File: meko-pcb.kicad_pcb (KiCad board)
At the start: 2 copper layers, 23 parts, among them IC1 ES9218PQ, IC2 AS5600-ASOM, IC3 TPS7A8701RTJT, IC4 TPS7A8701RTJT, J1 FH34SRJ-24S-0.5SH_99_, J2 MEM2090-00-145-00-A, J3 USB_C_Receptacle_USB2.0_16P, U1 ESP32-PICO-MINI-02, U12 BQ24075RGT, U4 CP2102N-Axx-xQFN20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

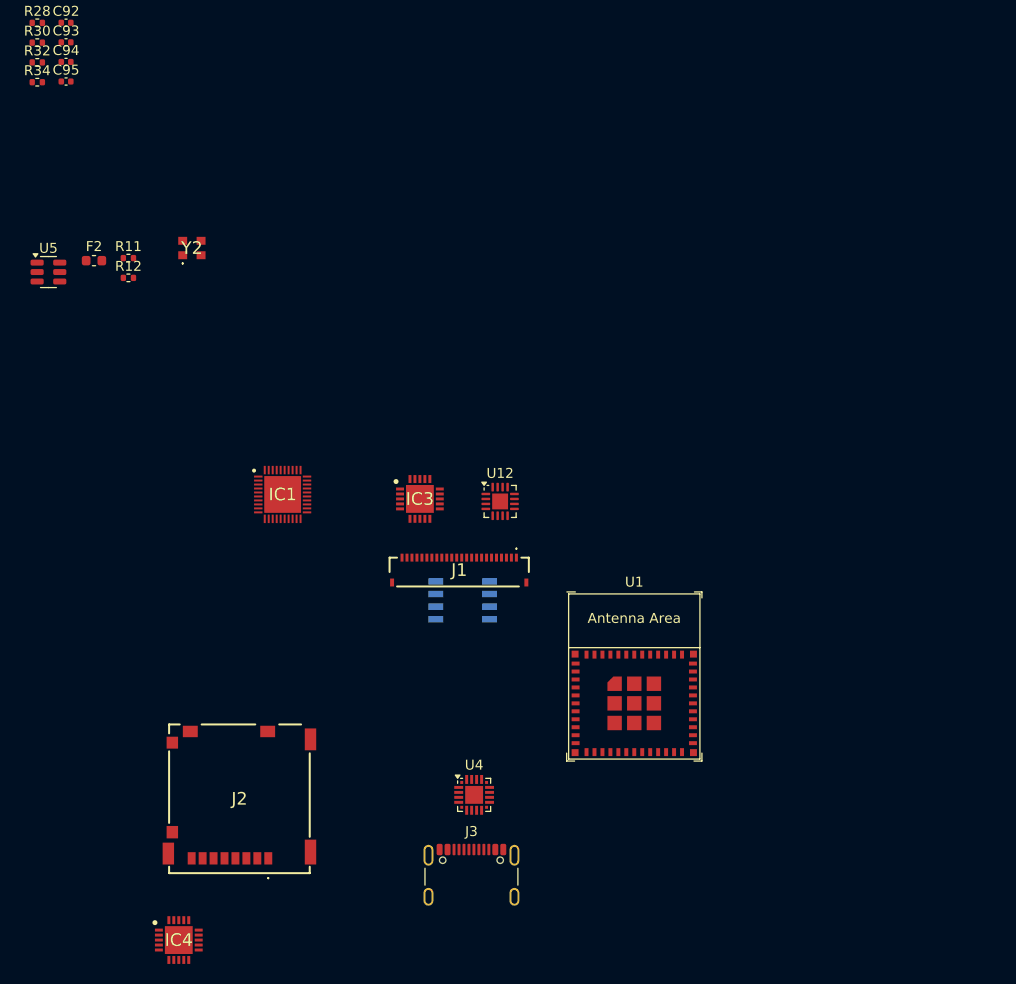
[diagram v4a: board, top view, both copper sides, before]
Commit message: re-did power with the new small LDOs and power system
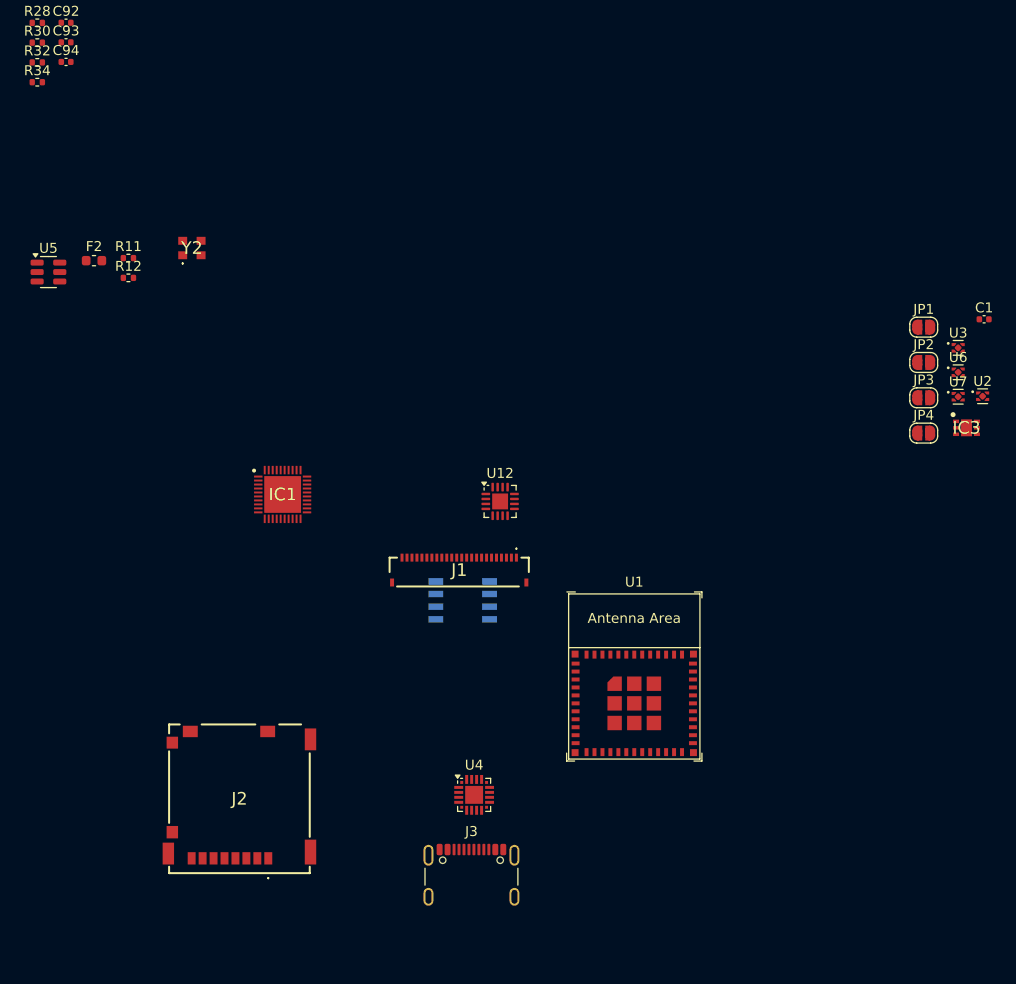
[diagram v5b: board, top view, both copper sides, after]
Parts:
- removed C95: 4.7uF, Capacitor_SMD:C_0402_1005Metric
- removed IC4: TPS7A8701RTJT, TPS7A8701RTJT:QFN50P400X400X80-21N-D
- added C1: 4.7uF, Capacitor_SMD:C_0402_1005Metric, F.Cu at (218.7, 91.9)
- added JP1: SolderJumper_2_Open, Jumper:SolderJumper-2_P1.3mm_Open_RoundedPad1.0x1.5mm, F.Cu at (212.7, 92.7)
- added JP2: SolderJumper_2_Open, Jumper:SolderJumper-2_P1.3mm_Open_RoundedPad1.0x1.5mm, F.Cu at (212.7, 96.3)
- added JP3: SolderJumper_2_Open, Jumper:SolderJumper-2_P1.3mm_Open_RoundedPad1.0x1.5mm, F.Cu at (212.7, 99.8)
- added JP4: SolderJumper_2_Open, Jumper:SolderJumper-2_P1.3mm_Open_RoundedPad1.0x1.5mm, F.Cu at (212.7, 103.4)
- added U2: LP5907SNX-1.8/NOPB, Package_SON:Texas_X2SON-4_1x1mm_P0.65mm, F.Cu at (218.6, 99.7)
- added U3: LP5907SNX-3.3/NOPB, Package_SON:Texas_X2SON-4_1x1mm_P0.65mm, F.Cu at (216.1, 94.8)
- added U6: LP5907SNX-3.3/NOPB, Package_SON:Texas_X2SON-4_1x1mm_P0.65mm, F.Cu at (216.1, 97.3)
- added U7: LP5907SNX-3.3/NOPB, Package_SON:Texas_X2SON-4_1x1mm_P0.65mm, F.Cu at (216.1, 99.7)
- IC3: value TPS7A8701RTJT -> LP5912-3.3DRVR; footprint TPS7A8701RTJT:QFN50P400X400X80-21N-D -> LP5912-3.3DRVR:SON65P200X200X80-7N
- moved IC3 55.4 mm to (216.9, 102.8)
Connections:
- IC3 pad 1: /power/REG-OUT -> +3V3
- IC3 pad 2: /power/REG-OUT -> unconnected-(IC3-NC-Pad2)
- IC3 pad 3: GND -> unconnected-(IC3-PG-Pad3)
- IC3 pad 5: /power/REG-OUT -> GND
- IC3 pad 6: unconnected-(IC3-EN2-Pad6) -> /power/REG-OUT
- IC3 pad 7: unconnected-(IC3-NR/SS2-Pad7) -> GND
- U1 pad 1: Net-(U1-GND-Pad1) -> GND
- U1 pad 11: Net-(U1-GND-Pad1) -> GND
- U1 pad 14: Net-(U1-GND-Pad1) -> GND
- U1 pad 2: Net-(U1-GND-Pad1) -> GND
- U1 pad 36: Net-(U1-GND-Pad1) -> GND
- U1 pad 37: Net-(U1-GND-Pad1) -> GND
- U1 pad 38: Net-(U1-GND-Pad1) -> GND
- U1 pad 39: Net-(U1-GND-Pad1) -> GND
- U1 pad 40: Net-(U1-GND-Pad1) -> GND
- U1 pad 41: Net-(U1-GND-Pad1) -> GND
- U1 pad 42: Net-(U1-GND-Pad1) -> GND
- U1 pad 43: Net-(U1-GND-Pad1) -> GND
- U1 pad 44: Net-(U1-GND-Pad1) -> GND
- U1 pad 45: Net-(U1-GND-Pad1) -> GND
- U1 pad 46: Net-(U1-GND-Pad1) -> GND
- U1 pad 47: Net-(U1-GND-Pad1) -> GND
- U1 pad 48: Net-(U1-GND-Pad1) -> GND
- U1 pad 49: Net-(U1-GND-Pad1) -> GND
- U1 pad 50: Net-(U1-GND-Pad1) -> GND
- U1 pad 51: Net-(U1-GND-Pad1) -> GND
- U1 pad 52: Net-(U1-GND-Pad1) -> GND
- U1 pad 53: Net-(U1-GND-Pad1) -> GND
- Y2 pad 4: +1V8 -> unconnected-(Y2-VDD-Pad4)

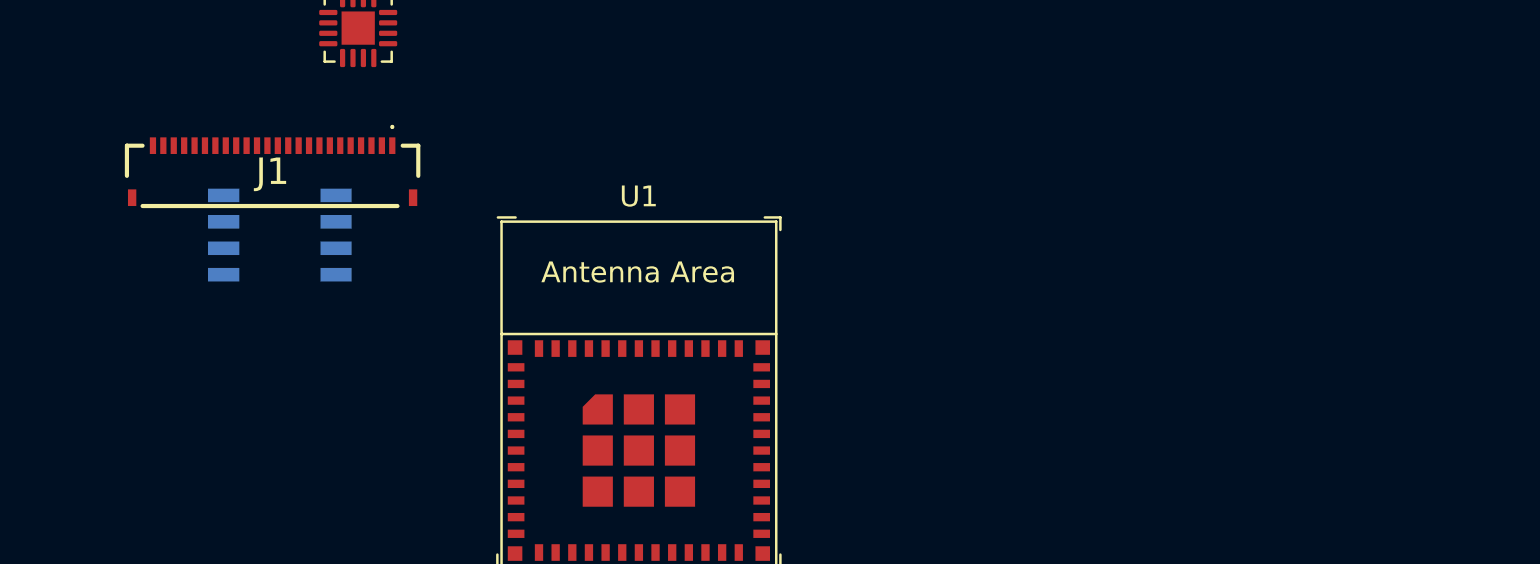
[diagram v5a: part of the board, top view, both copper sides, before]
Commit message: created custom symbol for the display, added pull-up/-down resistors
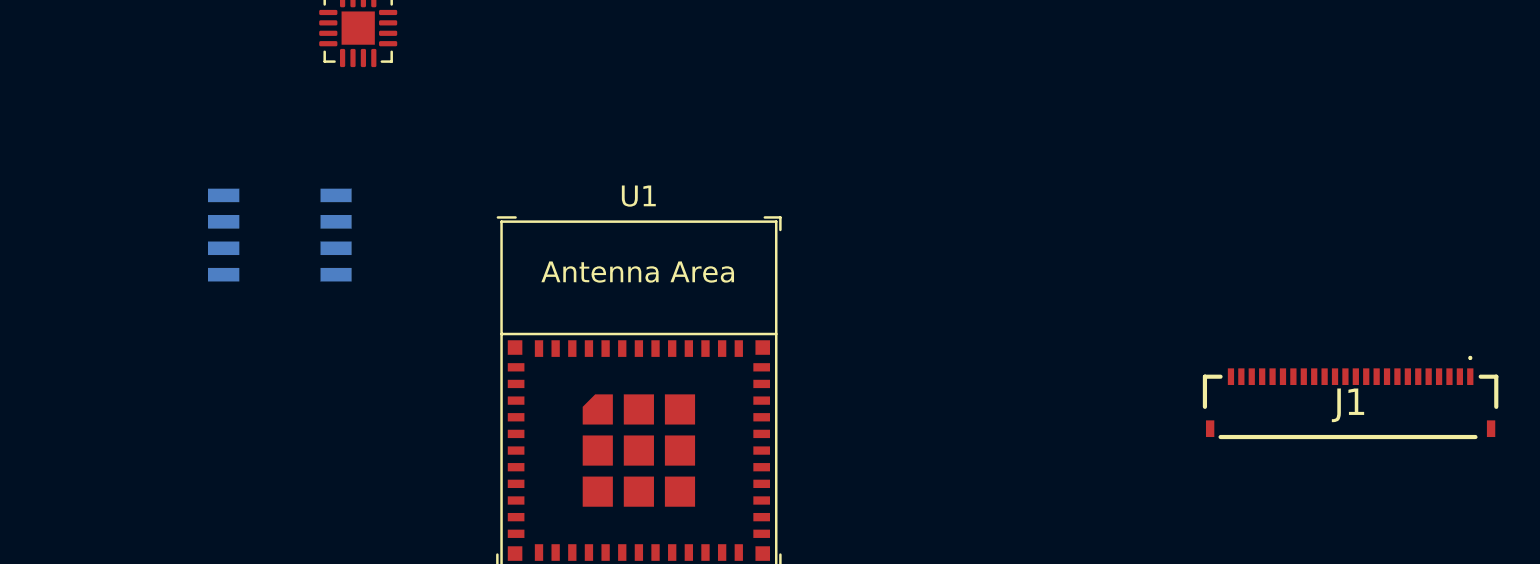
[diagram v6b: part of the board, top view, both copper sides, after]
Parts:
- J1: value FH34SRJ-24S-0.5SH_99_ -> GDEY0154D67
- moved J1 53.0 mm to (217.8, 128.4)
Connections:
- IC1 pad 19: +1V8 -> +1V8AVCC
- IC1 pad 20: +3V3 -> +3V3AVCC
- IC1 pad 29: +1V8 -> +3V3AVDD
- IC1 pad 4: +3V3 -> +3V3VCCA
- IC2 pad 2: unconnected-(IC2-VDD3V3-Pad2) -> +3V3
- J1 pad MP1: unconnected-(J1-PadMP1) -> GND
- J1 pad MP2: unconnected-(J1-PadMP2) -> GND
- J2 pad 10: unconnected-(J2-GROUND_1-Pad10) -> GND
- J2 pad 11: unconnected-(J2-GROUND_2-Pad11) -> GND
- J2 pad 12: unconnected-(J2-GROUND_3-Pad12) -> GND
- J2 pad 13: unconnected-(J2-GROUND_4-Pad13) -> GND
- J2 pad 14: unconnected-(J2-GROUND_5-Pad14) -> GND
- J2 pad 15: unconnected-(J2-GROUND_6-Pad15) -> GND
- U1 pad 3: unconnected-(U1-3V3-Pad3) -> +3V3
- Y2 pad 4: unconnected-(Y2-VDD-Pad4) -> +3V3MCLK

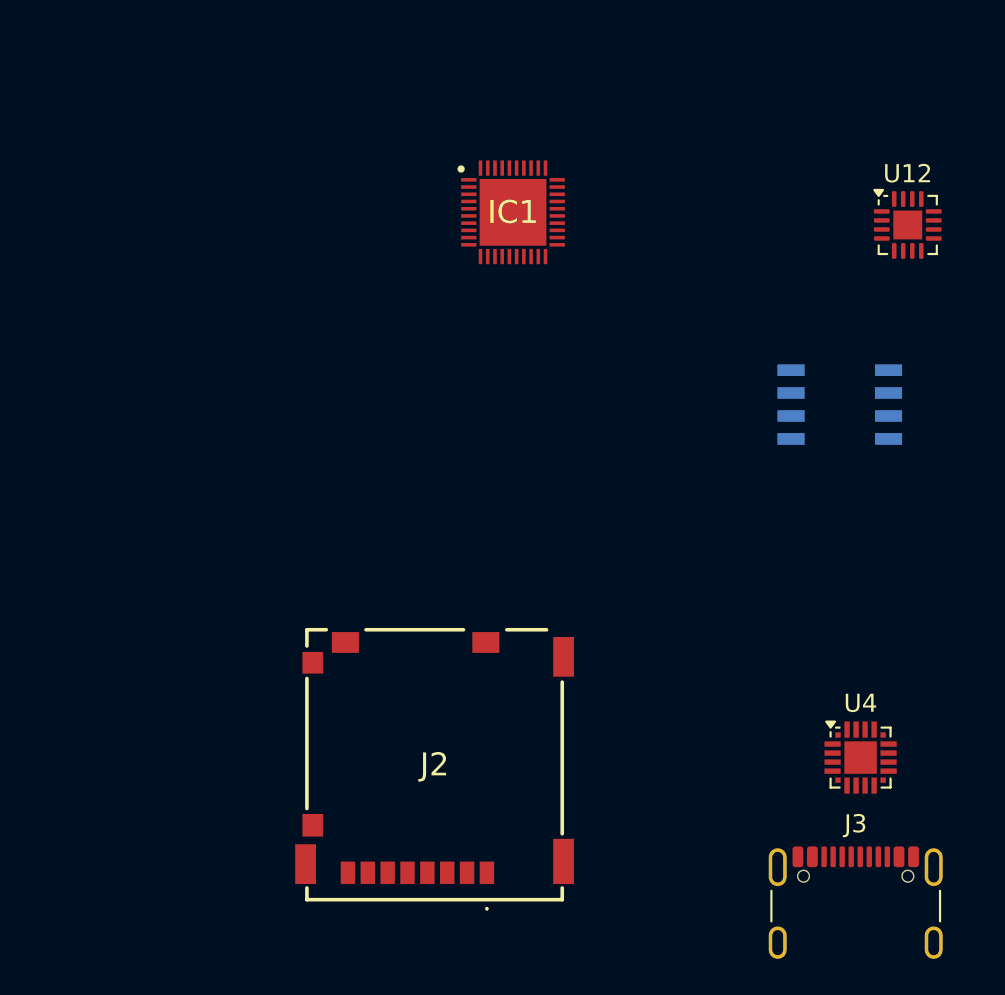
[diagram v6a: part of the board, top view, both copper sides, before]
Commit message: i2c, i2s, uart, en, sd card
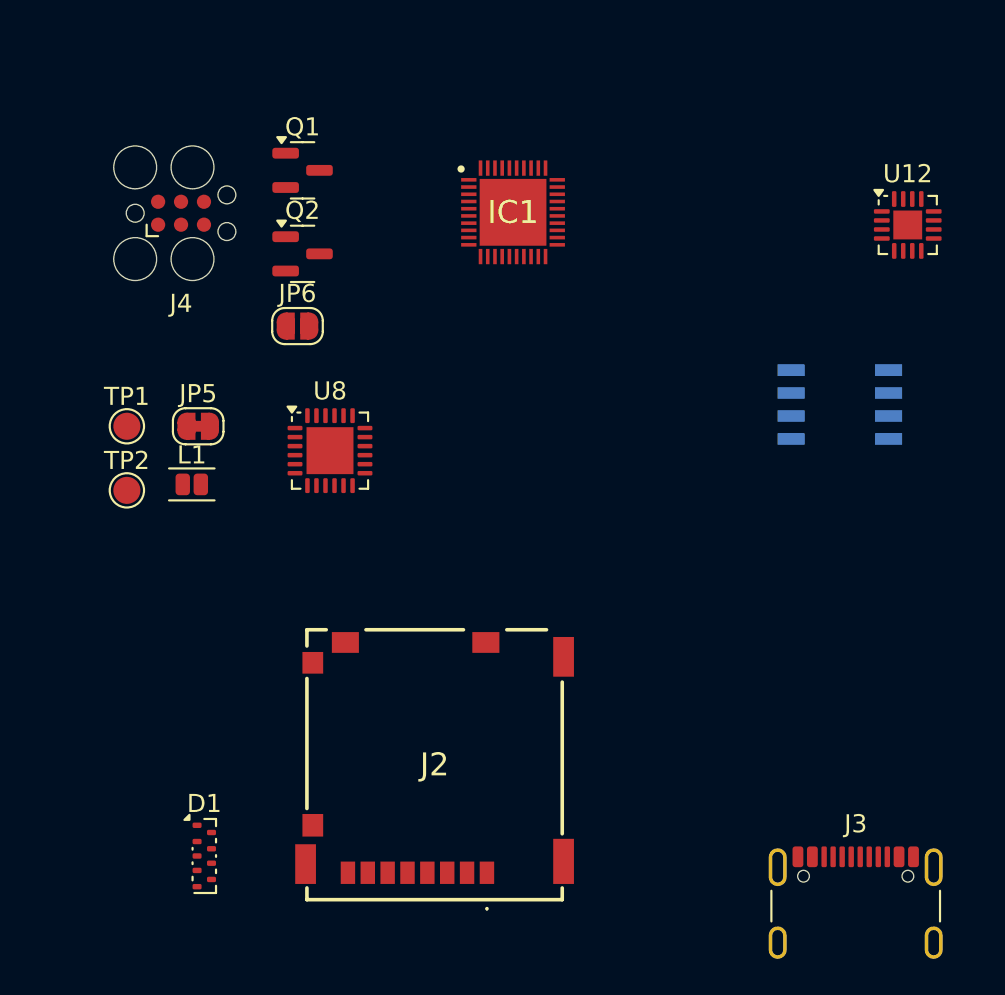
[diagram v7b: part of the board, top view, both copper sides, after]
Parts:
- removed U4: CP2102N-Axx-xQFN20, Package_DFN_QFN:SiliconLabs_QFN-20-1EP_3x3mm_P0.5mm_EP1.8x1.8mm
- added D1: D3V3X8U9LP3810, Package_DFN_QFN:Diodes_UDFN3810-9_TYPE_B, F.Cu at (131.1, 145.2)
- added J4: Conn_ARM_SWD_TagConnect_TC2030, Connector:Tag-Connect_TC2030-IDC-FP_2x03_P1.27mm_Vertical, F.Cu at (129.8, 109.6)
- added JP5: SolderJumper_2_Bridged, Jumper:SolderJumper-2_P1.3mm_Bridged_RoundedPad1.0x1.5mm, F.Cu at (130.8, 121.4)
- added JP6: SolderJumper_2_Open, Jumper:SolderJumper-2_P1.3mm_Open_RoundedPad1.0x1.5mm, F.Cu at (136.3, 115.8)
- added L1: 100uH, Inductor_SMD:L_TDK_MLZ2012_h1.25mm, F.Cu at (130.4, 124.6)
- added Q1: SS8050, Package_TO_SOT_SMD:SOT-23, F.Cu at (136.5, 107.2)
- added Q2: SS8050, Package_TO_SOT_SMD:SOT-23, F.Cu at (136.5, 111.8)
- added TP1: TestPoint, TestPoint:TestPoint_Pad_D1.5mm, F.Cu at (126.8, 121.4)
- added TP2: TestPoint, TestPoint:TestPoint_Pad_D1.5mm, F.Cu at (126.8, 125.0)
- added U8: CP2102N-Axx-xQFN24, Package_DFN_QFN:QFN-24-1EP_4x4mm_P0.5mm_EP2.6x2.6mm, F.Cu at (138.1, 122.8)
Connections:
- net /audio/DATA_CLK renamed /AUDIO_DATA_CLK
- IC1 pad 34: /audio/DATA_2 -> /AUDIO_DATA_2
- IC1 pad 35: /audio/DATA1 -> /AUDIO_DATA1
- IC1 pad 38: /audio/SCL -> /AUDIO_SCL
- IC1 pad 39: /audio/SDA -> /AUDIO_SDA
- IC2 pad 3: unconnected-(IC2-OUT-Pad3) -> /HAL_OUT
- IC2 pad 4: unconnected-(IC2-GND-Pad4) -> GND
- IC2 pad 5: unconnected-(IC2-PGO-Pad5) -> Net-(IC2-PGO)
- IC2 pad 6: unconnected-(IC2-SDA-Pad6) -> /HAL_SDA
- IC2 pad 7: unconnected-(IC2-SCL-Pad7) -> /HAL_SCL
- IC2 pad 8: unconnected-(IC2-DIR-Pad8) -> GND
- J2 pad 1: unconnected-(J2-DAT2-Pad1) -> /MEM_DAT2
- J2 pad 2: unconnected-(J2-CD/DAT3-Pad2) -> /MEM_DAT3
- J2 pad 3: unconnected-(J2-CMD-Pad3) -> /MEM_CMD
- J2 pad 4: unconnected-(J2-VDD-Pad4) -> +3V3
- J2 pad 5: unconnected-(J2-CLK-Pad5) -> /MEM_CLK
- J2 pad 6: unconnected-(J2-VSS-Pad6) -> GND
- J2 pad 7: unconnected-(J2-DAT0-Pad7) -> /MEM_DAT0
- J2 pad 8: unconnected-(J2-DAT1-Pad8) -> /MEM_DAT1
- J2 pad 9: unconnected-(J2-COM-Pad9) -> /MEM_COM
- U1 pad 15: unconnected-(U1-GPIO25/ADC2_CH8/DAC_1-Pad15) -> /AUDIO_SCL
- U1 pad 16: unconnected-(U1-GPIO26/ADC2_CH9/DAC_2-Pad16) -> /AUDIO_SDA
- U1 pad 18: unconnected-(U1-MTMS/GPIO14/ADC2_CH6-Pad18) -> /MEM_CLK
- U1 pad 19: unconnected-(U1-MTDI/GPIO12/ADC2_CH5-Pad19) -> /MEM_DAT2
- U1 pad 20: unconnected-(U1-MTCK/GPIO13/ADC2_CH4-Pad20) -> /MEM_DAT3
- U1 pad 21: unconnected-(U1-MTDO/GPIO15/ADC2_CH3-Pad21) -> /MEM_CMD
- U1 pad 22: unconnected-(U1-GPIO2/ADC2_CH2-Pad22) -> /MEM_DAT0
- U1 pad 23: unconnected-(U1-GPIO0/BOOT/ADC2_CH1-Pad23) -> /BOOT
- U1 pad 24: unconnected-(U1-GPIO4/ADC2_CH0-Pad24) -> /MEM_DAT1
- U1 pad 26: unconnected-(U1-GPIO20-Pad26) -> /HAL_SDA
- U1 pad 30: unconnected-(U1-U0RXD/GPIO3-Pad30) -> /RXD
- U1 pad 31: unconnected-(U1-U0TXD/GPIO1-Pad31) -> /TXD
- U1 pad 33: unconnected-(U1-GPIO19-Pad33) -> /HAL_SCL
- U1 pad 34: unconnected-(U1-GPIO22-Pad34) -> /AUDIO_DATA_2
- U1 pad 35: unconnected-(U1-GPIO21-Pad35) -> /AUDIO_DATA1
- U1 pad 4: unconnected-(U1-SENSOR_VP/GPIO36/ADC1_CH0-Pad4) -> /HAL_OUT
- U1 pad 8: unconnected-(U1-EN/CHIP_PU-Pad8) -> /ESP_EN
- U12 pad 6: +5V -> Net-(JP5-B)
- U12 pad 7: unconnected-(U12-~{PGOOD}-Pad7) -> Net-(U12-~{PGOOD})
- U12 pad 9: unconnected-(U12-~{CHG}-Pad9) -> Net-(U12-~{CHG})

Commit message: finishing up schematic
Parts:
- added D2: MBR0530, Diode_SMD:D_SOD-123, F.Cu at (202.3, 118.5)
- added D3: MBR0530, Diode_SMD:D_SOD-123, F.Cu at (245.2, 126.9)
- added D4: MBR0530, Diode_SMD:D_SOD-123, F.Cu at (245.2, 130.3)
- added J5: SJ2-35954B-SMT-TR, SJ2-35954B-SMT-TR:CUI_SJ2-35954B-SMT-TR, F.Cu at (76.8, 74.8)
- added JP7: SolderJumper_2_Bridged, Jumper:SolderJumper-2_P1.3mm_Bridged_RoundedPad1.0x1.5mm, F.Cu at (125.3, 146.0)
- added JP8: SolderJumper_2_Bridged, Jumper:SolderJumper-2_P1.3mm_Bridged_RoundedPad1.0x1.5mm, F.Cu at (240.1, 130.6)
- added JP9: SolderJumper_2_Bridged, Jumper:SolderJumper-2_P1.3mm_Bridged_RoundedPad1.0x1.5mm, F.Cu at (70.2, 82.3)
- added L2: 47uF, Inductor_SMD:L_TDK_MLZ2012_h1.25mm, F.Cu at (239.7, 133.8)
- added Q3: Si1308EDL, Package_TO_SOT_SMD:SOT-323_SC-70, F.Cu at (244.5, 134.0)
- added TP10: TestPoint, TestPoint:TestPoint_Pad_D1.5mm, F.Cu at (77.0, 91.5)
- added TP11: TestPoint, TestPoint:TestPoint_Pad_D1.5mm, F.Cu at (77.0, 95.0)
- added TP12: TestPoint, TestPoint:TestPoint_Pad_D1.5mm, F.Cu at (80.5, 87.9)
- added TP13: TestPoint, TestPoint:TestPoint_Pad_D1.5mm, F.Cu at (80.5, 91.5)
- added TP14: TestPoint, TestPoint:TestPoint_Pad_D1.5mm, F.Cu at (80.5, 95.0)
- added TP3: TestPoint, TestPoint:TestPoint_Pad_D1.5mm, F.Cu at (69.8, 87.9)
- added TP4: TestPoint, TestPoint:TestPoint_Pad_D1.5mm, F.Cu at (69.8, 91.5)
- added TP5: TestPoint, TestPoint:TestPoint_Pad_D1.5mm, F.Cu at (69.8, 95.0)
- added TP6: TestPoint, TestPoint:TestPoint_Pad_D1.5mm, F.Cu at (73.4, 87.9)
- added TP7: TestPoint, TestPoint:TestPoint_Pad_D1.5mm, F.Cu at (73.4, 91.5)
- added TP8: TestPoint, TestPoint:TestPoint_Pad_D1.5mm, F.Cu at (73.4, 95.0)
- added TP9: TestPoint, TestPoint:TestPoint_Pad_D1.5mm, F.Cu at (77.0, 87.9)
- JP1, JP2, JP3, JP4: value SolderJumper_2_Open -> SolderJumper_2_Bridged; footprint Jumper:SolderJumper-2_P1.3mm_Open_RoundedPad1.0x1.5mm -> Jumper:SolderJumper-2_P1.3mm_Bridged_RoundedPad1.0x1.5mm
- moved JP1 126.4 mm to (88.0, 71.3)
- moved JP2 126.4 mm to (88.0, 74.9)
- moved JP3 126.4 mm to (88.0, 78.4)
- moved JP4 126.4 mm to (88.0, 82.0)
- moved R34 57.9 mm to (164.0, 109.5)
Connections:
- IC1 pad 37: /audio/RESETB -> /AUDIO_RESETB
- IC2 pad 1: unconnected-(IC2-VDD5V-Pad1) -> Net-(IC2-VDD5V)
- J1 pad 10: unconnected-(J1-~{RES}-Pad10) -> /DISPL_~{RES}
- J1 pad 11: unconnected-(J1-~{D/C}-Pad11) -> /DISPL_~{D/C}
- J1 pad 12: unconnected-(J1-~{CS}-Pad12) -> /DISPL_~{CS}
- J1 pad 13: unconnected-(J1-SCL-Pad13) -> /DISPL_SCL
- J1 pad 14: unconnected-(J1-SDA-Pad14) -> /DISPL_SDA
- J1 pad 15: unconnected-(J1-VDDIO-Pad15) -> +3V3
- J1 pad 16: unconnected-(J1-VCI-Pad16) -> +3V3
- J1 pad 17: unconnected-(J1-VSS-Pad17) -> GND
- J1 pad 18: unconnected-(J1-VDD-Pad18) -> Net-(J1-VDD)
- J1 pad 2: unconnected-(J1-GDR-Pad2) -> /DISPL_GDR
- J1 pad 20: unconnected-(J1-VSH1-Pad20) -> Net-(J1-VSH1)
- J1 pad 21: unconnected-(J1-VGH-Pad21) -> /DISPL_PREVGH
- J1 pad 22: unconnected-(J1-VSL-Pad22) -> /DISPL_PREVSL
- J1 pad 23: unconnected-(J1-VGL-Pad23) -> /DISPL_PREVGL
- J1 pad 24: unconnected-(J1-VCOM-Pad24) -> /DISPL_VCOM
- J1 pad 3: unconnected-(J1-RESE-Pad3) -> /DISPL_RESE
- J1 pad 5: unconnected-(J1-VSH2-Pad5) -> Net-(J1-VSH2)
- J1 pad 8: unconnected-(J1-BS1-Pad8) -> GND
- J1 pad 9: unconnected-(J1-BUSY-Pad9) -> /DISPL_BUSY
- Q2 pad 3: /BOOT -> /AUDIO_DATA_CLK
- U1 pad 10: unconnected-(U1-VDET_2/GPIO35/ADC1_CH7-Pad10) -> /BTN_PWR
- U1 pad 13: unconnected-(U1-32K_XN/GPIO33/ADC1_CH5-Pad13) -> /AUDIO_MLCK_EN
- U1 pad 17: unconnected-(U1-GPIO27/ADC2_CH7-Pad17) -> /DISPL_SCL
- U1 pad 23: /BOOT -> /AUDIO_DATA_CLK
- U1 pad 27: unconnected-(U1-SD_DATA_0/GPIO7-Pad27) -> /MEM_COM
- U1 pad 28: unconnected-(U1-SD_DATA_1/GPIO8-Pad28) -> /DISPL_SDA
- U1 pad 29: unconnected-(U1-GPIO5-Pad29) -> /BTN_SIDE_R
- U1 pad 5: unconnected-(U1-SENSOR_CAPP/GPIO37/ADC1_CH1-Pad5) -> /BTN_VOL_DWN
- U1 pad 6: unconnected-(U1-SENSOR_CAPN/GPIO38/ADC1_CH2-Pad6) -> /BTN_SIDE_L
- U1 pad 7: unconnected-(U1-SENSOR_VN/GPIO39/ADC1_CH3-Pad7) -> /AUDIO_RESETB
- U1 pad 9: unconnected-(U1-VDET_1/GPIO34/ADC1_CH6-Pad9) -> /BTN_VOL_UP
- Y2 pad 1: /audio/MCLK_EN -> /AUDIO_MLCK_EN
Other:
- board outline added: 258.5 x 149 mm
